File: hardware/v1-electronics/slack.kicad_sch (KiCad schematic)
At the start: 0 parts

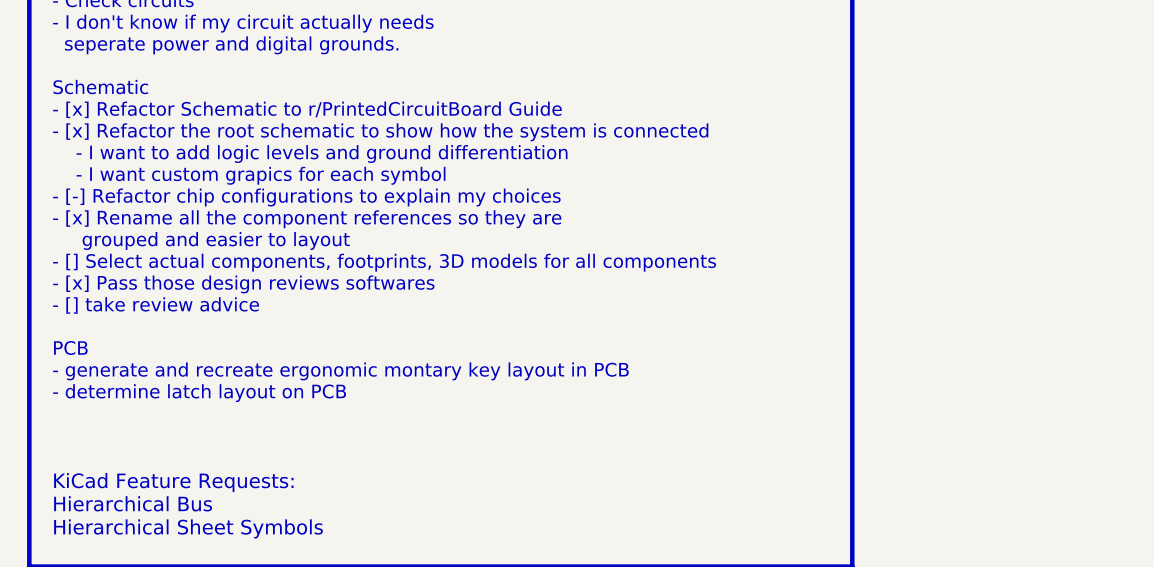
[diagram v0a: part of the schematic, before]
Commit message: feat(v1 hardware): add all components
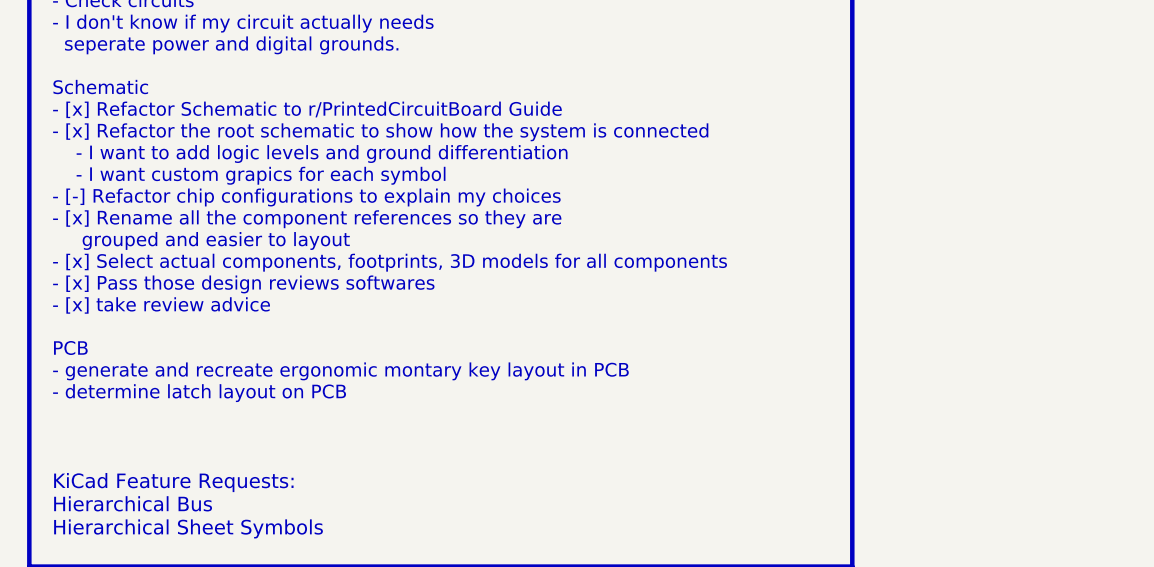
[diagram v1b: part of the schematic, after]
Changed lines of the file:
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@@
 		)
 	)
-	(text "- Check circuits\n- I don't know if my circuit actually needs\n  seperate power and digital grounds.\n\nSchematic\n- [x] Refactor Schematic to r/PrintedCircuitBoard Guide\n- [x] Refactor the root schematic to show how the system is connected\n	- I want to add logic levels and ground differentiation\n	- I want custom grapics for each symbol\n- [-] Refactor chip configurations to explain my choices\n- [x] Rename all the component references so they are\n     grouped and easier to layout\n- [] Select actual components, footprints, 3D models for all components\n- [x] Pass those design reviews softwares\n- [] take review advice\n\nPCB\n- generate and recreate ergonomic montary key layout in PCB\n- determine latch layout on PCB"
+	(text "- Check circuits\n- I don't know if my circuit actually needs\n  seperate power and digital grounds.\n\nSchematic\n- [x] Refactor Schematic to r/PrintedCircuitBoard Guide\n- [x] Refactor the root schematic to show how the system is connected\n	- I want to add logic levels and ground differentiation\n	- I want custom grapics for each symbol\n- [-] Refactor chip configurations to explain my choices\n- [x] Rename all the component references so they are\n     grouped and easier to layout\n- [x] Select actual components, footprints, 3D models for all components\n- [x] Pass those design reviews softwares\n- [x] take review advice\n\nPCB\n- generate and recreate ergonomic montary key layout in PCB\n- determine latch layout on PCB"
 		(exclude_from_sim no)
 		(at 17.78 137.16 0)

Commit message: feat(v1 hardware): transfer to ergogen layout
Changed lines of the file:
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@@
 		(title "Slack")
 		(date "2026-07-25")
-		(rev "A.0.5")
+		(rev "A.0.7")
 	)
 	(rectangle
@@
 		)
 	)
-	(text "- Check circuits\n- I don't know if my circuit actually needs\n  seperate power and digital grounds.\n\nSchematic\n- [x] Refactor Schematic to r/PrintedCircuitBoard Guide\n- [x] Refactor the root schematic to show how the system is connected\n	- I want to add logic levels and ground differentiation\n	- I want custom grapics for each symbol\n- [-] Refactor chip configurations to explain my choices\n- [x] Rename all the component references so they are\n     grouped and easier to layout\n- [x] Select actual components, footprints, 3D models for all components\n- [x] Pass those design reviews softwares\n- [x] take review advice\n\nPCB\n- generate and recreate ergonomic montary key layout in PCB\n- determine latch layout on PCB"
+	(text "- Check circuits\n- I don't know if my circuit actually needs\n  seperate power and digital grounds.\n\nSchematic\n- [x] Refactor Schematic to r/PrintedCircuitBoard Guide\n- [x] Refactor the root schematic to show how the system is connected\n	- I want to add logic levels and ground differentiation\n	- I want custom grapics for each symbol\n- [-] Refactor chip configurations to explain my choices\n- [x] Rename all the component references so they are\n     grouped and easier to layout\n- [x] Select actual components, footprints, 3D models for all components\n- [x] Pass those design reviews softwares\n- [x] take review advice\n- [ ] remove the outer switches from the thumb clusters"
 		(exclude_from_sim no)
 		(at 17.78 137.16 0)
